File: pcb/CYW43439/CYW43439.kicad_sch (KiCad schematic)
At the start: 31 parts, among them J1 GPIOs, J2 SPI, J3 Power, U1 CYW43439KUBGT, Y1 Crystal

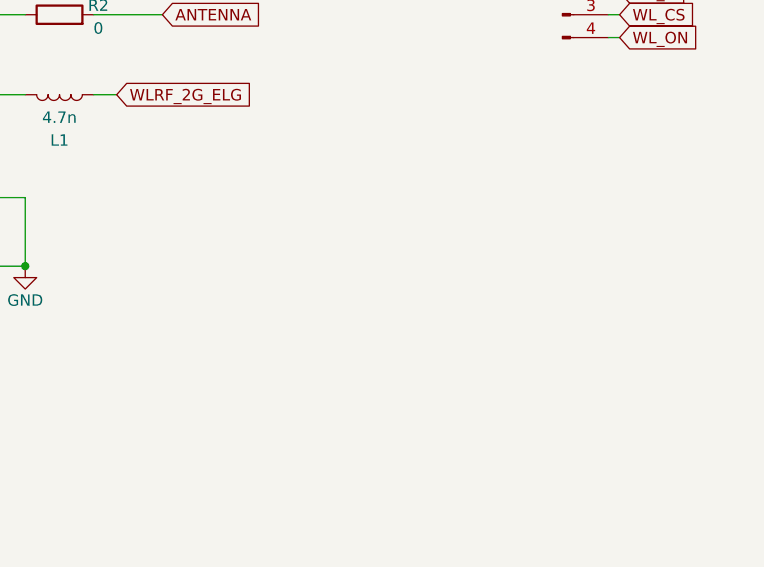
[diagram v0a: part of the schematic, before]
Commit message: [pcb] move rev2 into dedicated folder + start new rev
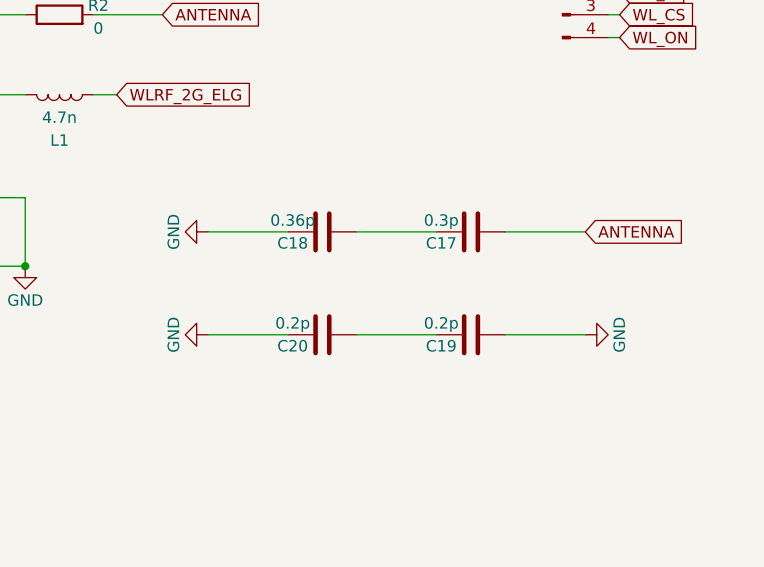
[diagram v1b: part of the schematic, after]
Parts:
- added C17: 0.3p, Capacitor_SMD:C_0402_1005Metric, symbol Device:C
- added C18: 0.36p, Capacitor_SMD:C_0402_1005Metric, symbol Device:C
- added C19, C20: 0.2p, Capacitor_SMD:C_0402_1005Metric, symbol Device:C
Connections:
- net ANTENNA: now also C17.1
- net GND: now also C18.2, C19.1, C20.2
- new net: C19.2, C20.1
- new net: C17.2, C18.1
